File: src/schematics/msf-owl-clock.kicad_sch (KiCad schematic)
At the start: 38 parts, among them U001 BC805M

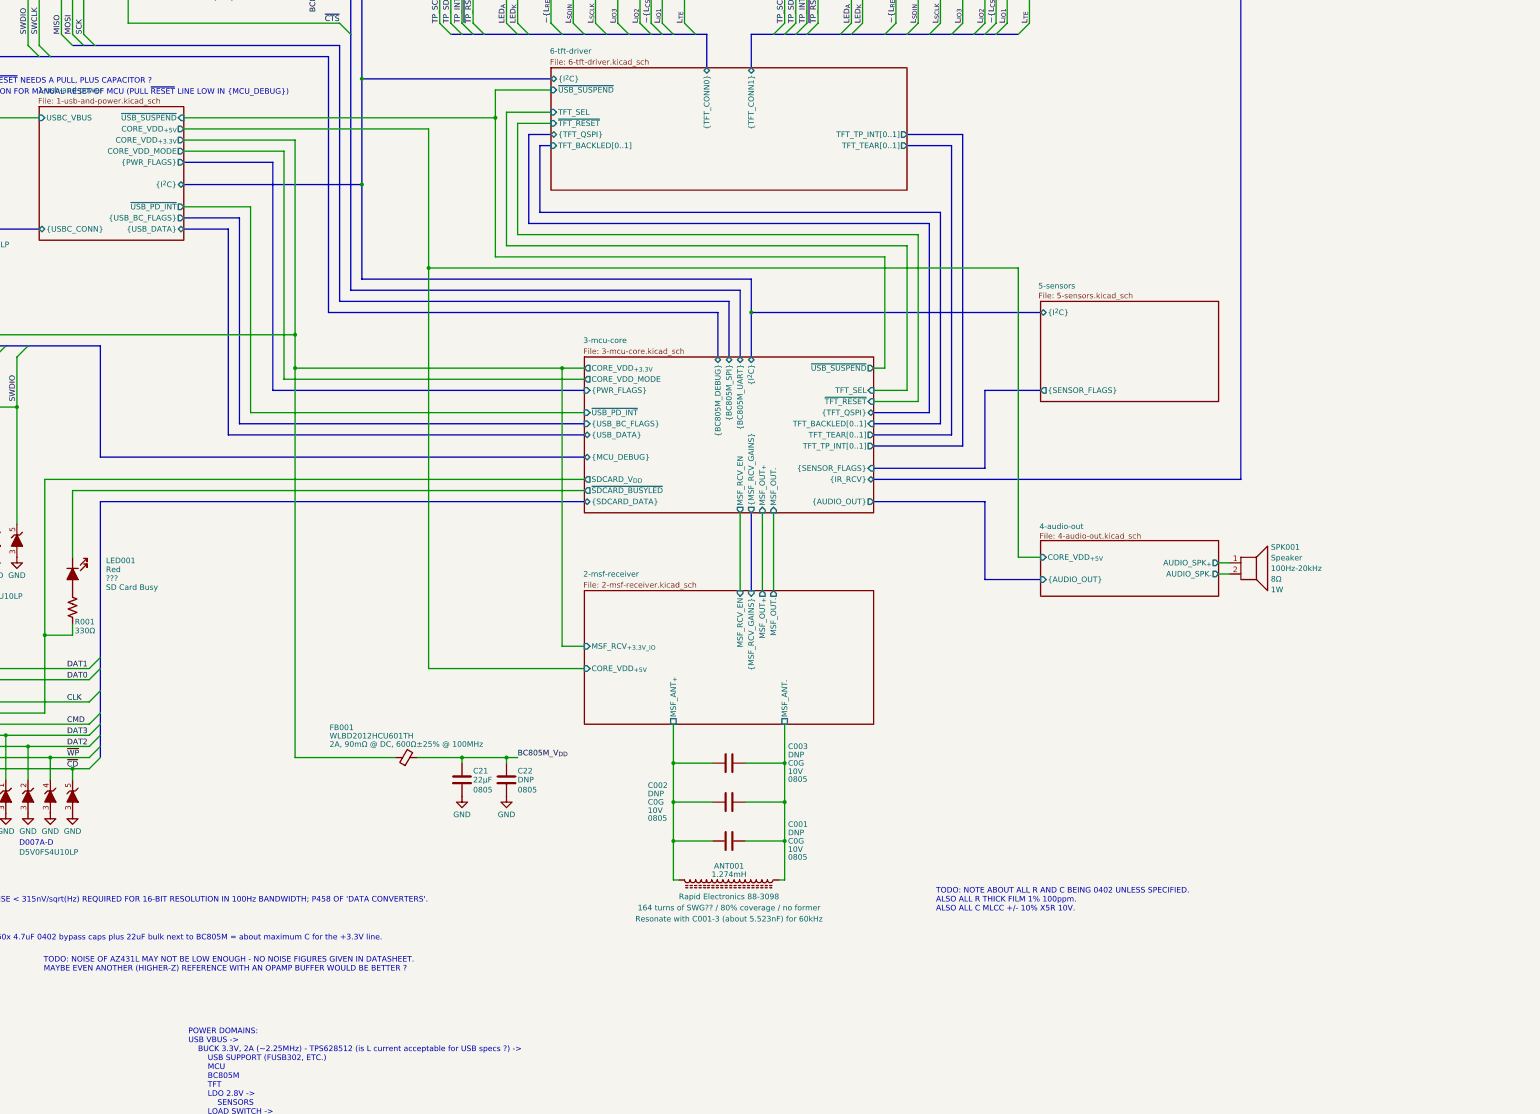
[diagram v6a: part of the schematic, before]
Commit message: Further elaboration of the USB / Power schematic.
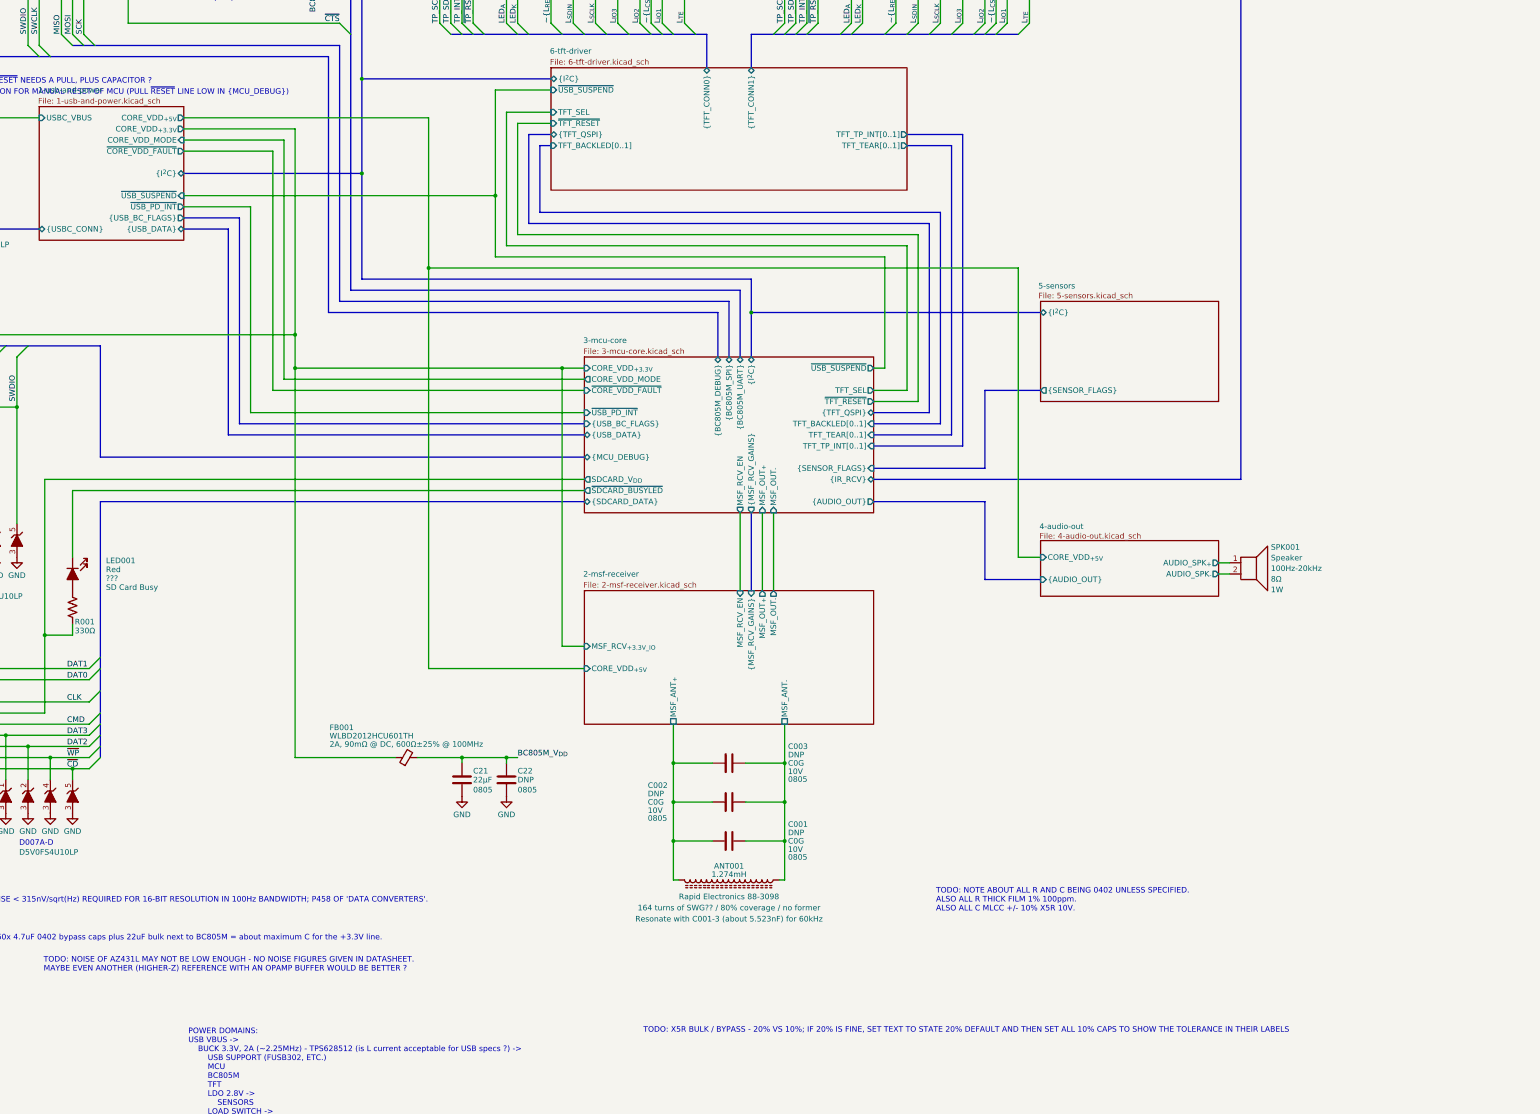
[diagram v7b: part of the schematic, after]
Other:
- sheet 1-usb-and-power ports: added ~{CORE_VDD_FAULT}; removed {PWR_FLAGS}
- sheet 3-mcu-core ports: added ~{CORE_VDD_FAULT}; removed {PWR_FLAGS}
- note added: "TODO: X5R BULK / BYPASS - 20% VS 10%; IF 20% IS FINE, SET TEXT TO STATE 20% DEFAULT AND THEN SET ALL 10% CAPS TO SHOW THE TOLERANCE IN THEIR LABELS"
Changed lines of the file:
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@@
   (junction (at 73.66 163.83) (diameter 0) (color 0 0 0 0)
   )
-  (junction (at 172.72 97.79) (diameter 0) (color 0 0 0 0)
-  )
   (junction (at 81.28 215.9) (diameter 0) (color 0 0 0 0)
   )
+  (junction (at 203.2 100.33) (diameter 0) (color 0 0 0 0)
+  )
   (junction (at 106.68 231.14) (diameter 0) (color 0 0 0 0)
   )
@@
   (junction (at 243.84 247.65) (diameter 0) (color 0 0 0 0)
   )
+  (junction (at 172.72 95.25) (diameter 0) (color 0 0 0 0)
+  )
   (junction (at 53.34 33.02) (diameter 0) (color 0 0 0 0)
   )
@@
   (junction (at 58.42 35.56) (diameter 0) (color 0 0 0 0)
   )
-  (junction (at 203.2 82.55) (diameter 0) (color 0 0 0 0)
-  )
-  (junction (at 187.96 116.84) (diameter 0) (color 0 0 0 0)
-  )
   (junction (at 172.72 73.66) (diameter 0) (color 0 0 0 0)
   )
@@
   (junction (at 53.34 101.6) (diameter 0) (color 0 0 0 0)
   )
+  (junction (at 187.96 116.84) (diameter 0) (color 0 0 0 0)
+  )
   (junction (at 96.52 226.06) (diameter 0) (color 0 0 0 0)
   )
@@
     (stroke (width 0) (type default))
   )
-  (wire (pts (xy 203.2 82.55) (xy 203.2 76.2))
-    (stroke (width 0) (type default))
-  )
   (wire (pts (xy 96.52 33.02) (xy 127 33.02))
     (stroke (width 0) (type default))
@@
     (stroke (width 0) (type default))
   )
+  (wire (pts (xy 152.4 144.78) (xy 223.52 144.78))
+    (stroke (width 0) (type default))
+  )
   (wire (pts (xy 180.34 228.6) (xy 157.48 228.6))
     (stroke (width 0) (type default))
@@
     (stroke (width 0) (type default))
   )
-  (bus (pts (xy 172.72 97.79) (xy 172.72 119.38))
+  (bus (pts (xy 172.72 95.25) (xy 172.72 119.38))
     (stroke (width 0) (type default))
   )
@@
     (stroke (width 0) (type default))
   )
+  (wire (pts (xy 203.2 76.2) (xy 203.2 100.33))
+    (stroke (width 0) (type default))
+  )
   (wire (pts (xy 299.72 48.26) (xy 299.72 60.96))
     (stroke (width 0) (type default))
   )
-  (wire (pts (xy 132.08 82.55) (xy 203.2 82.55))
+  (wire (pts (xy 132.08 100.33) (xy 203.2 100.33))
     (stroke (width 0) (type default))
   )
@@
     (stroke (width 0) (type default))
   )
-  (bus (pts (xy 172.72 73.66) (xy 172.72 97.79))
+  (bus (pts (xy 172.72 73.66) (xy 172.72 95.25))
     (stroke (width 0) (type default))
   )
@@
     (stroke (width 0) (type default))
   )
-  (wire (pts (xy 187.96 85.09) (xy 187.96 116.84))
-    (stroke (width 0) (type default))
-  )
-  (wire (pts (xy 187.96 116.84) (xy 187.96 208.28))
+  (wire (pts (xy 187.96 82.55) (xy 187.96 116.84))
     (stroke (width 0) (type default))
   )
@@
     (stroke (width 0) (type default))
   )
-  (wire (pts (xy 154.94 142.24) (xy 154.94 90.17))
+  (wire (pts (xy 154.94 142.24) (xy 154.94 87.63))
     (stroke (width 0) (type default))
   )
@@
     (stroke (width 0) (type default))
   )
-  (bus (pts (xy 152.4 144.78) (xy 223.52 144.78))
-    (stroke (width 0) (type default))
-  )
   (wire (pts (xy 78.74 137.16) (xy 78.74 158.75))
     (stroke (width 0) (type default))
@@
     (stroke (width 0) (type default))
   )
-  (wire (pts (xy 132.08 87.63) (xy 157.48 87.63))
+  (wire (pts (xy 132.08 85.09) (xy 157.48 85.09))
     (stroke (width 0) (type default))
   )
@@
     (stroke (width 0) (type default))
   )
-  (wire (pts (xy 157.48 87.63) (xy 157.48 132.08))
+  (wire (pts (xy 157.48 85.09) (xy 157.48 132.08))
     (stroke (width 0) (type default))
   )
@@
     (stroke (width 0) (type default))
   )
-  (bus (pts (xy 132.08 97.79) (xy 172.72 97.79))
+  (bus (pts (xy 132.08 95.25) (xy 172.72 95.25))
     (stroke (width 0) (type default))
   )
@@
     (stroke (width 0) (type default))
   )
-  (bus (pts (xy 132.08 92.71) (xy 152.4 92.71))
-    (stroke (width 0) (type default))
-  )
   (bus (pts (xy 261.62 63.5) (xy 266.7 63.5))
     (stroke (width 0) (type default))
@@
     (stroke (width 0) (type default))
   )
-  (wire (pts (xy 203.2 114.3) (xy 203.2 82.55))
+  (wire (pts (xy 203.2 114.3) (xy 203.2 100.33))
     (stroke (width 0) (type default))
   )
@@
     (stroke (width 0) (type default))
   )
-  (wire (pts (xy 132.08 85.09) (xy 187.96 85.09))
+  (wire (pts (xy 132.08 82.55) (xy 187.96 82.55))
     (stroke (width 0) (type default))
   )
@@
     (stroke (width 0) (type default))
   )
+  (wire (pts (xy 132.08 90.17) (xy 152.4 90.17))
+    (stroke (width 0) (type default))
+  )
   (wire (pts (xy 287.02 48.26) (xy 287.02 60.96))
     (stroke (width 0) (type default))
@@
     (stroke (width 0) (type default))
   )
+  (wire (pts (xy 187.96 116.84) (xy 187.96 208.28))
+    (stroke (width 0) (type default))
+  )
   (bus (pts (xy 113.03 205.74) (xy 113.03 208.28))
     (stroke (width 0) (type default))
@@
     (stroke (width 0) (type default))
   )
+  (wire (pts (xy 152.4 90.17) (xy 152.4 144.78))
+    (stroke (width 0) (type default))
+  )
   (bus (pts (xy 144.78 152.4) (xy 144.78 105.41))
     (stroke (width 0) (type default))
@@
     (stroke (width 0) (type default))
   )
-  (wire (pts (xy 154.94 90.17) (xy 132.08 90.17))
+  (wire (pts (xy 154.94 87.63) (xy 132.08 87.63))
     (stroke (width 0) (type default))
   )
@@
     (stroke (width 0) (type default))
   )
-  (bus (pts (xy 152.4 92.71) (xy 152.4 144.78))
-    (stroke (width 0) (type default))
-  )
   (text "D006A-D" (at 74.168 248.92 0)
     (effects (font (size 1.27 1.27)) (justify left bottom))
   )
+  (text "TODO: X5R BULK / BYPASS - 20% VS 10%; IF 20% IS FINE, SET TEXT TO STATE 20% DEFAULT AND THEN SET ALL 10% CAPS TO SHOW THE TOLERANCE IN THEIR LABELS"
+    (at 236.982 291.592 0)
+    (effects (font (size 1.27 1.27)) (justify left bottom))
+  )
   (text "D002A-D" (at 78.74 110.49 0)
     (effects (font (size 1.27 1.27)) (justify left bottom))
@@
       (effects (font (size 1.27 1.27)) (justify left top))
     )
-    (pin "{I^{2}C}" bidirectional (at 132.08 97.79 0)
+    (pin "{I^{2}C}" bidirectional (at 132.08 95.25 0)
       (effects (font (size 1.27 1.27)) (justify right))
     )
@@
       (effects (font (size 1.27 1.27)) (justify right))
     )
-    (pin "{PWR_FLAGS}" output (at 132.08 92.71 0)
-      (effects (font (size 1.27 1.27)) (justify right))
-    )
     (pin "~{USB_PD_INT}" output (at 132.08 102.87 0)
       (effects (font (size 1.27 1.27)) (justify right))
@@
       (effects (font (size 1.27 1.27)) (justify right))
     )
-    (pin "CORE_VDD_{+3.3V}" output (at 132.08 87.63 0)
+    (pin "CORE_VDD_{+3.3V}" output (at 132.08 85.09 0)
+      (effects (font (size 1.27 1.27)) (justify right))
+    )
+    (pin "CORE_VDD_{+5V}" output (at 132.08 82.55 0)
       (effects (font (size 1.27 1.27)) (justify right))
     )
-    (pin "CORE_VDD_{+5V}" output (at 132.08 85.09 0)
+    (pin "CORE_VDD_MODE" input (at 132.08 87.63 0)
       (effects (font (size 1.27 1.27)) (justify right))
     )
-    (pin "CORE_VDD_MODE" output (at 132.08 90.17 0)
+    (pin "~{USB_SUSPEND}" input (at 132.08 100.33 0)
       (effects (font (size 1.27 1.27)) (justify right))
     )
-    (pin "~{USB_SUSPEND}" input (at 132.08 82.55 0)
+    (pin "~{CORE_VDD_FAULT}" output (at 132.08 90.17 0)
       (effects (font (size 1.27 1.27)) (justify right))
     )
@@
       (effects (font (size 1.27 1.27)) (justify right))
     )
-    (pin "CORE_VDD_{+3.3V}" output (at 223.52 139.7 180)
+    (pin "CORE_VDD_{+3.3V}" input (at 223.52 139.7 180)
       (effects (font (size 1.27 1.27)) (justify left))
     )
@@
       (effects (font (size 1.27 1.27)) (justify right))
     )
-    (pin "TFT_TEAR[0..1]" output (at 289.56 154.94 0)
+    (pin "TFT_TEAR[0..1]" input (at 289.56 154.94 0)
       (effects (font (size 1.27 1.27)) (justify right))
     )
@@
       (effects (font (size 1.27 1.27)) (justify right))
     )
-    (pin "TFT_SEL" input (at 289.56 144.78 0)
+    (pin "TFT_SEL" output (at 289.56 144.78 0)
       (effects (font (size 1.27 1.27)) (justify right))
     )
-    (pin "~{TFT_RESET}" input (at 289.56 147.32 0)
+    (pin "~{TFT_RESET}" output (at 289.56 147.32 0)
       (effects (font (size 1.27 1.27)) (justify right))
     )
-    (pin "TFT_TP_INT[0..1]" output (at 289.56 157.48 0)
+    (pin "TFT_TP_INT[0..1]" input (at 289.56 157.48 0)
       (effects (font (size 1.27 1.27)) (justify right))
     )
@@
       (effects (font (size 1.27 1.27)) (justify right))
     )
-    (pin "{PWR_FLAGS}" input (at 223.52 144.78 180)
-      (effects (font (size 1.27 1.27)) (justify left))
-    )
     (pin "~{USB_PD_INT}" input (at 223.52 149.86 180)
       (effects (font (size 1.27 1.27)) (justify left))
@@
       (effects (font (size 1.27 1.27)) (justify left))
     )
+    (pin "~{CORE_VDD_FAULT}" input (at 223.52 144.78 180)
+      (effects (font (size 1.27 1.27)) (justify left))
+    )

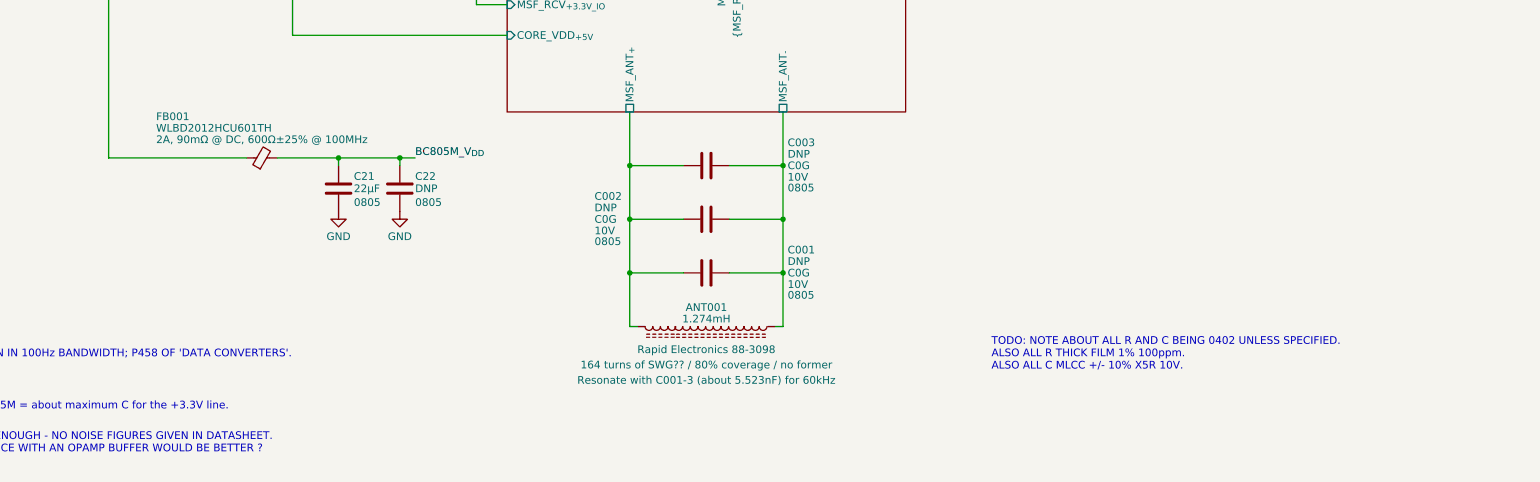
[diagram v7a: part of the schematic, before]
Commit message: Further elaboration of the USB / power module schematics.
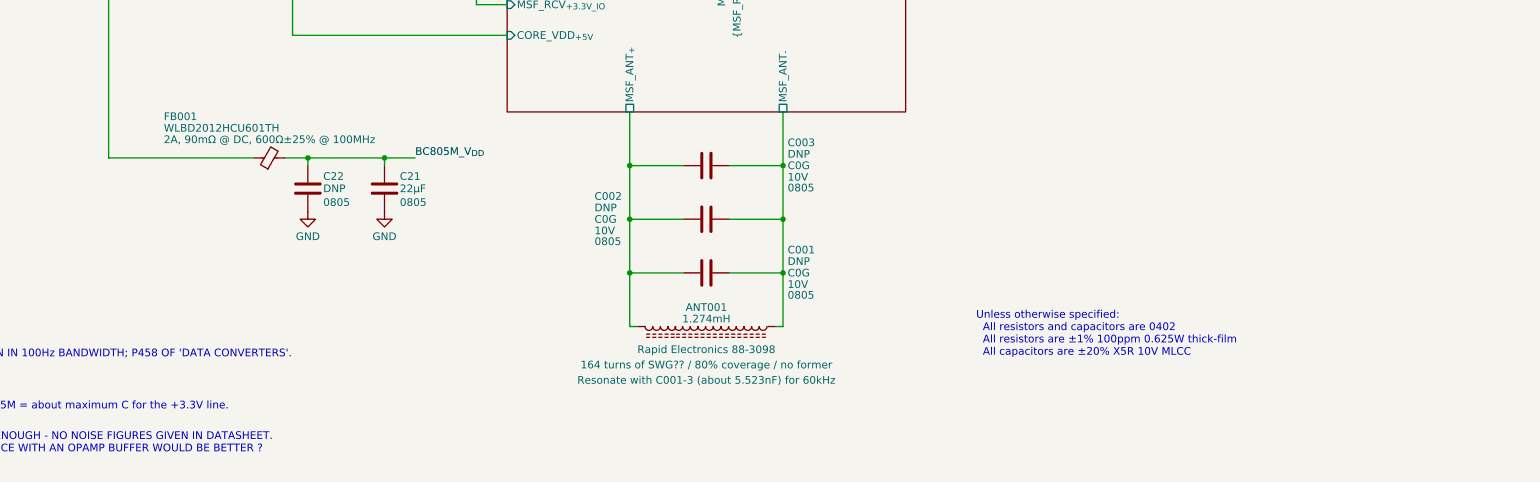
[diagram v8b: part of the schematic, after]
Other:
- note added: "Unless otherwise specified: All resistors and capacitors are 0402 All resistors are ±1% 100ppm 0.625W thick-film All capacitors are ±20% X5R 10V MLCC"
- note removed: "TODO: NOTE ABOUT ALL R AND C BEING 0402 UNLESS SPECIFIED. ALSO ALL R THICK FILM 1% 100ppm. ALSO ALL C MLCC +/- 10% X5R 10V."
- moved on the sheet: C21, C22, FB001
